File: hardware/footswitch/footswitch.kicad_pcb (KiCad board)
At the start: 2 copper layers, 34 x 58 mm, 6 parts, among them J1 Conn_02x05_Counter_Clockwise

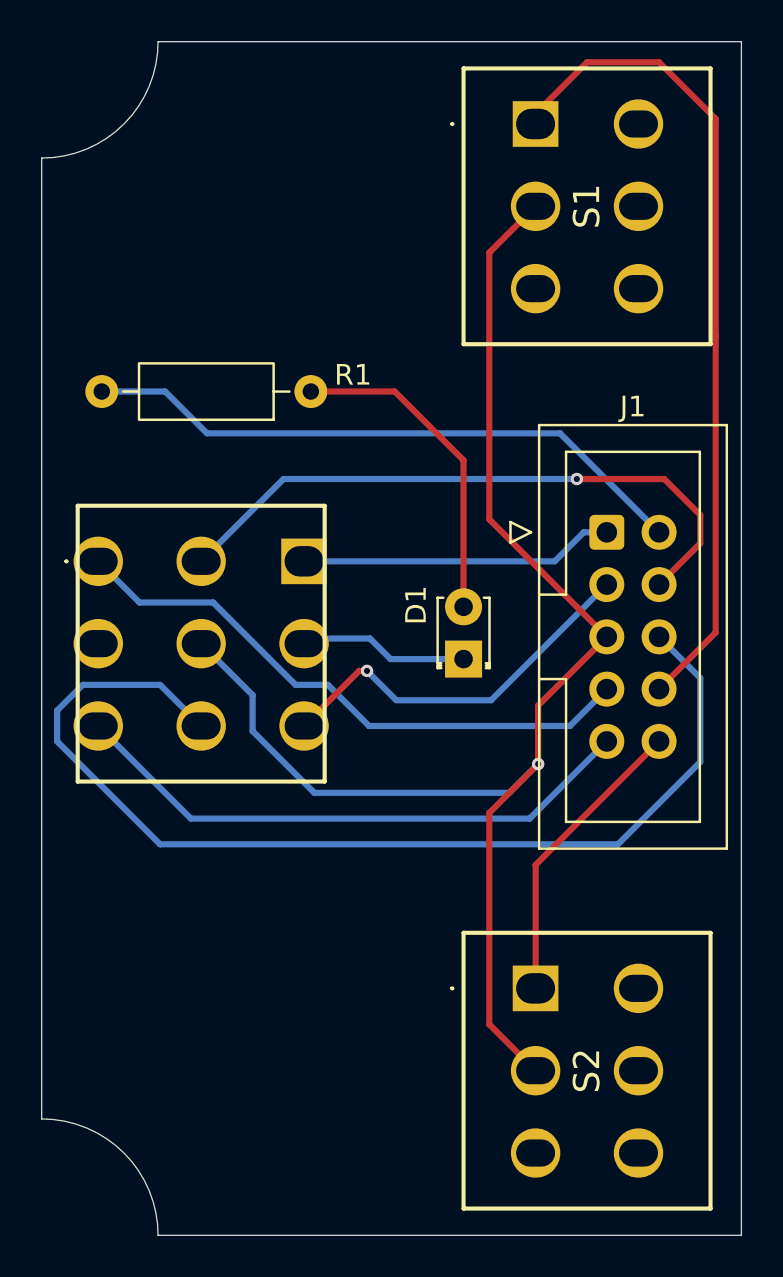
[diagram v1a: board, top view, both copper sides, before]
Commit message: Fix pad nums on 3dpdt footprint and rotate on board
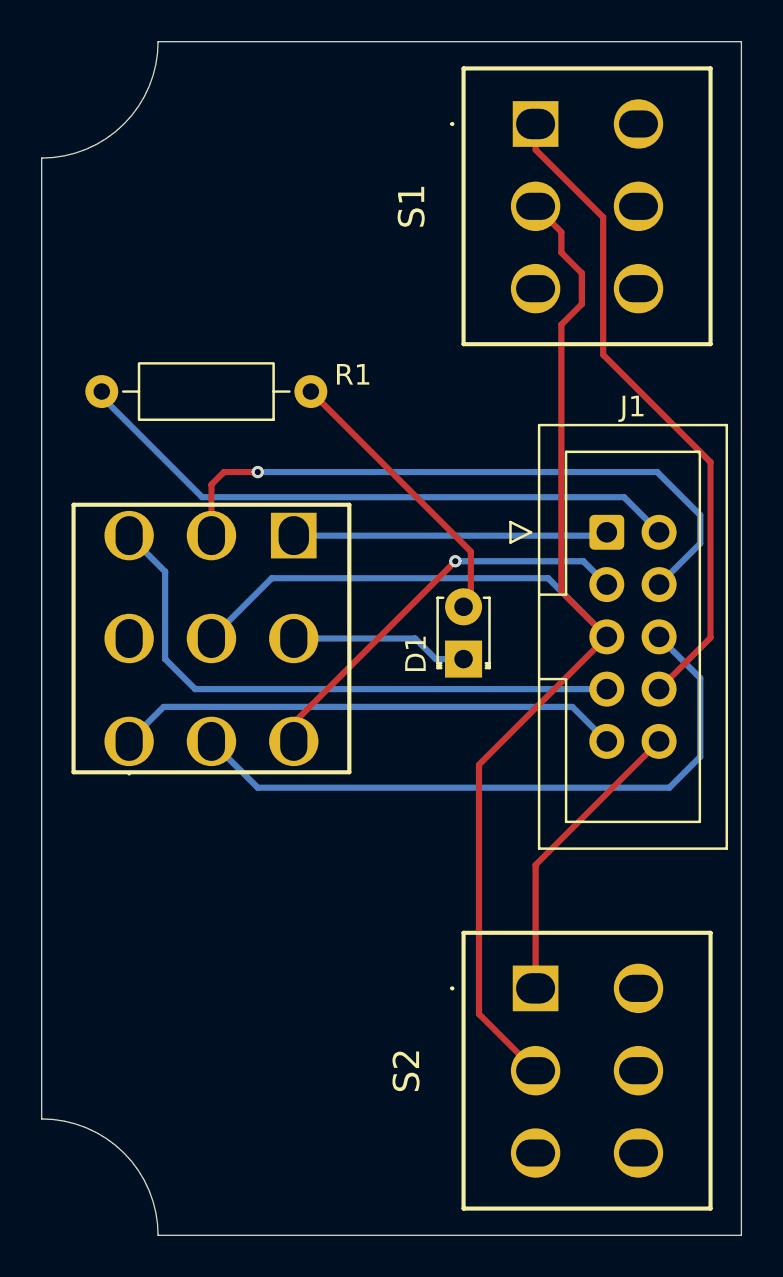
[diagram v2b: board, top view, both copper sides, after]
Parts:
- moved 3DPDT Footswitch1 6.33 mm to (134.2, 96.5), turned to 0 degrees
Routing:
- net /conn6: track 51.7 -> 32.0 mm
- net /conn8: track 40.3 -> 32.0 mm
- net /conn9: track 28.1 -> 24.6 mm
- net Net-(D1-A): track 15.9 -> 13.8 mm
- net /fsw2: track 6.91 -> 8.66 mm
- net /conn4: track 30.8 -> 31.6 mm
- net /conn3: track 19.3 -> 19.8 mm
- net /conn5: vias 1 -> 0
